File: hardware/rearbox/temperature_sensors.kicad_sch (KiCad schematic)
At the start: 15 parts

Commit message: Changed power section
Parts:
- gave numbers to parts that had none: 9
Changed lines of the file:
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@@
 (kicad_sch
-	(version 20231120)
+	(version 20250114)
 	(generator "eeschema")
-	(generator_version "8.0")
+	(generator_version "9.0")
 	(paper "A4")
 	(title_block
@@
 		(comment 1 "Reviewer:")
 	)
+	(text "G = 2\nR_{F} = 4k7\nR_{G} = 4k7"
+		(exclude_from_sim no)
+		(at 234.95 69.85 0)
+		(effects
+			(font
+				(size 1.27 1.27)
+			)
+			(justify left bottom)
+		)
+	)
+	(text "G = 2\nR_{F} = 4k7\nR_{G} = 4k7"
+		(exclude_from_sim no)
+		(at 234.95 146.05 0)
+		(effects
+			(font
+				(size 1.27 1.27)
+			)
+			(justify left bottom)
+		)
+	)
+	(text "NTC\n2k"
+		(exclude_from_sim no)
+		(at 178.435 59.055 0)
+		(effects
+			(font
+				(size 1.27 1.27)
+			)
+			(justify right bottom)
+		)
+	)
+	(text "NTC\n2k"
+		(exclude_from_sim no)
+		(at 178.435 97.155 0)
+		(effects
+			(font
+				(size 1.27 1.27)
+			)
+			(justify right bottom)
+		)
+	)
+	(text "G = 2\nR_{F} = 4k7\nR_{G} = 4k7"
+		(exclude_from_sim no)
+		(at 234.95 107.95 0)
+		(effects
+			(font
+				(size 1.27 1.27)
+			)
+			(justify left bottom)
+		)
+	)
+	(text "NTC\n2k"
+		(exclude_from_sim no)
+		(at 178.435 135.255 0)
+		(effects
+			(font
+				(size 1.27 1.27)
+			)
+			(justify right bottom)
+		)
+	)
+	(text_box "Resistance range:\n2480 to 435 Ω\n(20 to 70 °C)\n\nOptimum value of the upper resistor in the divider:\nR = sqrt(2480 * 435) ≈ 1 kΩ\n\nOutput range:\n0.237 V to 1.867 V"
+		(exclude_from_sim no)
+		(at 22.86 134.62 0)
+		(size 31.75 22.86)
+		(margins 0.9524 0.9524 0.9524 0.9524)
+		(stroke
+			(width -0.0001)
+			(type default)
+		)
+		(fill
+			(type none)
+		)
+		(effects
+			(font
+				(size 1.27 1.27)
+			)
+			(justify left top)
+		)
+	)
+	(text_box "Sensor: Bosch 0 261 230 340\nOEM ID: SH01-18-541\nRange: -40 °C to 140 °C\n\nhttps://www.efisolutions.com.au/bosch-fluid-pressure-and-temperature-sensor-pst-f1"
+		(exclude_from_sim no)
+		(at 22.86 115.57 0)
+		(size 90.17 11.43)
+		(margins 0.9524 0.9524 0.9524 0.9524)
+		(stroke
+			(width -0.0001)
+			(type default)
+		)
+		(fill
+			(type none)
+		)
+		(effects
+			(font
+				(size 1.27 1.27)
+			)
+			(justify left top)
+		)
+	)
 	(junction
 		(at 195.58 52.07)
@@
 			"AAAAAEASAOEOAAAAAABAEgDhDgAAAAAAQBIA4Q4AAAAAAEASAOEOAAAAAABAEgDhDgAAAAAAQBIA"
 			"4Q4AAAAAAEASAOEOAAAAAABAEgDhDgAAAAAAQBIA4Q4AAAAAAEASAOEOAAAAAABAEgDhDgAAAAAA"
-			"QBLw/9uJrOufjjWHAAAAAElFTkSuQmCC"
-		)
-	)
-	(text_box "Resistance range:\n2480 to 435 Ω\n(20 to 70 °C)\n\nOptimum value of the upper resistor in the divider:\nR = sqrt(2480 * 435) ≈ 1 kΩ\n\nOutput range:\n0.237 V to 1.867 V"
-		(exclude_from_sim no)
-		(at 22.86 134.62 0)
-		(size 31.75 22.86)
-		(stroke
-			(width -0.0001)
-			(type default)
-		)
-		(fill
-			(type none)
-		)
-		(effects
-			(font
-				(size 1.27 1.27)
-			)
-			(justify left top)
-		)
-	)
-	(text_box "Sensor: Bosch 0 261 230 340\nOEM ID: SH01-18-541\nRange: -40 °C to 140 °C\n\nhttps://www.efisolutions.com.au/bosch-fluid-pressure-and-temperature-sensor-pst-f1"
-		(exclude_from_sim no)
-		(at 22.86 115.57 0)
-		(size 90.17 11.43)
-		(stroke
-			(width -0.0001)
-			(type default)
-		)
-		(fill
-			(type none)
-		)
-		(effects
-			(font
-				(size 1.27 1.27)
-			)
-			(justify left top)
-		)
-	)
-	(text "G = 2\nR_{F} = 4k7\nR_{G} = 4k7"
-		(exclude_from_sim no)
-		(at 234.95 69.85 0)
-		(effects
-			(font
-				(size 1.27 1.27)
-			)
-			(justify left bottom)
-		)
-	)
-	(text "G = 2\nR_{F} = 4k7\nR_{G} = 4k7"
-		(exclude_from_sim no)
-		(at 234.95 146.05 0)
-		(effects
-			(font
-				(size 1.27 1.27)
-			)
-			(justify left bottom)
-		)
-	)
-	(text "NTC\n2k"
-		(exclude_from_sim no)
-		(at 178.435 59.055 0)
-		(effects
-			(font
-				(size 1.27 1.27)
-			)
-			(justify right bottom)
-		)
-	)
-	(text "NTC\n2k"
-		(exclude_from_sim no)
-		(at 178.435 97.155 0)
-		(effects
-			(font
-				(size 1.27 1.27)
-			)
-			(justify right bottom)
-		)
-	)
-	(text "G = 2\nR_{F} = 4k7\nR_{G} = 4k7"
-		(exclude_from_sim no)
-		(at 234.95 107.95 0)
-		(effects
-			(font
-				(size 1.27 1.27)
-			)
-			(justify left bottom)
-		)
-	)
-	(text "NTC\n2k"
-		(exclude_from_sim no)
-		(at 178.435 135.255 0)
-		(effects
-			(font
-				(size 1.27 1.27)
-			)
-			(justify right bottom)
+			"QBLw/9uJrOufjjWHAAAAAElFTkSuQmCCMQBwAFgAbABnAHcAdwA2AFEAbQBaAG4ATQBUAGwAZwBu"
+			"AEwARAB3ADgATQBwAFIAMgBzAG0AWQBGAEUAQQBpAHAATgBPAFAASQByAFMATgBJAHkAcQBqAFIA"
+			"YQBGAGUAVABaAEQAawBKAEQASwBEAEUAQQB6AGcAYQBWAGYAVgB5AEsAUwBKAHoAcAA5ACsANgAy"
+			"AHEANQBrAEMAUAB0AGgAeQBWAGcATwBUAEkAcwAvAGkAbgBUADMAdwB1AEoAVgBUAFoAcwBhAHgA"
+			"bQBMAE0AVABiADMAbgBiAEoAVwBlAGMAYwBTAGQAbABCAGoATQBXAFEASwBLADYAagBJAEUAbABM"
+			"AEMAVABRAG8AYQBHAG8ATgAyAEsAaABoAGEATgA2ADgANABrAFAAWAB2AEgAWABwAEUAawBiAEMA"
+			"cgBEAFIATABaAHAAWQBVAEUAUAB6AHcAQgArAHYAdgB1AEgAMgAxAFcAdAAwADcAUAA0ADUANwBM"
+			"AG4AbgA3AFoAbgB2ADMATAAwADEAVQBPADMANQBSAHQAZABCAFYAUQBHAEcAbQBKAFYAagA3AEYA"
+			"OQBLAHoAaQBsAEkAQgB0AFIAeABiAFoAbAA4AHIATgArACsAcQBqAHEAQwBFAGQAbABLADEAMgB0"
+			"ADQAVAB4AGMAWQAzAEgAUABoAGQAcwB0AC8AWgBDADMAcwBTAHIAWABlADEAbgBKAGkANwBtAGgA"
+			"UQBKAEgAdQArACsAcwA2AFAAcQBMAGEAUQBRAGgAYQBaAEEANgAvAHYAYgB2AC8AMwBzADgARABC"
+			"AEsAaABTAFAARgBRAGcATQAxAEIAaQB4AGIASwBuAC8ALwBzAFgAZQBjAGQAOQA3AHgATQBXAHcA"
+			"VAAyAFMANwBZAEwAaAB5AEcARABSAE8AagBRAFUAYgBOAGQAZwBSAHUAQgA3AGMAVgBjAGYAcwBM"
+			"AEwAagByAHAAQQB4ADkAOAAzAGYAUgBwAEkARQBHAHgAVgB0AGsAUwBnAFIARgBsAGkAUQBkAFgA"
+			"bABWAC8AKwA4AHIAZgBCAEsAYQBxAGkAbwBQAE0AcABxAHcAYgBwADcAYgBQAFYAYgB0ACsAOQBN"
+			"AHYARgBrAFYAcABlAEMAVABmAHMARwBTAEcALwA2AGMAcwBKAGQAYQBvAGMAdQBPADEAbABxAEsA"
+			"dwBwAEgARAArAHEAVABzAFIALwBtADkAKwAxADUAcwArAE4AeAB6AGsAUgBLADIAZABmADAAZABB"
+			"AFMASQBwAFUAdAByAGYALwBmAFIAZAB4ADUANQA1AEoASQBnAFcAOABGAHQASQBqAHMAQwBSAHMA"
+			"MQBHAFkAQwBQAEMARQBjAG8AUQBiAA=="
 		)
 	)
 	(label "N3"
 		(at 218.44 132.08 180)
-		(fields_autoplaced yes)
 		(effects
 			(font
@@
 	(label "N3"
 		(at 185.42 128.27 180)
-		(fields_autoplaced yes)
 		(effects
 			(font
@@
 	(label "N2"
 		(at 185.42 90.17 180)
-		(fields_autoplaced yes)
 		(effects
 			(font
@@
 	(label "P2"
 		(at 190.5 90.17 0)
-		(fields_autoplaced yes)
 		(effects
 			(font
@@
 	(label "N2"
 		(at 218.44 93.98 180)
-		(fields_autoplaced yes)
 		(effects
 			(font
@@
 	(label "N1"
 		(at 218.44 55.88 180)
-		(fields_autoplaced yes)
 		(effects
 			(font
@@
 	(label "N1"
 		(at 185.42 52.07 180)
-		(fields_autoplaced yes)
 		(effects
 			(font
@@
 	(label "P1"
 		(at 218.44 49.53 180)
-		(fields_autoplaced yes)
 		(effects
 			(font
@@
 	(label "P3"
 		(at 190.5 128.27 0)
-		(fields_autoplaced yes)
 		(effects
 			(font
@@
 	(label "P2"
 		(at 218.44 87.63 180)
-		(fields_autoplaced yes)
 		(effects
 			(font
@@
 	(label "P3"
 		(at 218.44 125.73 180)
-		(fields_autoplaced yes)
 		(effects
 			(font
@@
 	(label "P1"
 		(at 190.5 52.07 0)
-		(fields_autoplaced yes)
 		(effects
 			(font
@@
 		(shape output)
 		(at 252.73 125.73 0)
-		(fields_autoplaced yes)
 		(effects
 			(font
@@
 		(shape input)
 		(at 173.99 128.27 180)
-		(fields_autoplaced yes)
 		(effects
 			(font
@@
 		(shape output)
 		(at 252.73 49.53 0)
-		(fields_autoplaced yes)
 		(effects
 			(font
@@
 		(shape input)
 		(at 173.99 90.17 180)
-		(fields_autoplaced yes)
 		(effects
 			(font
@@
 		(shape output)
 		(at 252.73 87.63 0)
-		(fields_autoplaced yes)
 		(effects
 			(font
@@
 		(shape input)
 		(at 173.99 52.07 180)
-		(fields_autoplaced yes)
 		(effects
 			(font
@@
 		(on_board yes)
 		(dnp no)
-		(property "Reference" "R?"
+		(property "Reference" "R100"
 			(at 197.358 120.7516 0)
 			(effects
@@
 		(on_board yes)
 		(dnp no)
-		(property "Reference" "R?"
+		(property "Reference" "R95"
 			(at 178.562 120.7516 0)
 			(effects
@@
 		(on_board yes)
 		(dnp no)
-		(property "Reference" "R?"
+		(property "Reference" "R94"
 			(at 178.562 82.6516 0)
 			(effects
@@
 		(on_board yes)
 		(dnp no)
-		(property "Reference" "R?"
+		(property "Reference" "R98"
 			(at 197.358 82.6516 0)
 			(effects
@@
 		(on_board yes)
 		(dnp no)
-		(property "Reference" "#PWR?"
+		(property "Reference" "#PWR0192"
 			(at 187.96 68.58 0)
 			(effects
@@
 		(on_board yes)
 		(dnp no)
-		(property "Reference" "#PWR?"
+		(property "Reference" "#PWR0196"
 			(at 187.96 144.78 0)
 			(effects
@@
 		(on_board yes)
 		(dnp no)
-		(property "Reference" "R?"
+		(property "Reference" "R97"
 			(at 197.358 54.7116 0)
 			(effects
@@
 		(on_board yes)
 		(dnp no)
-		(property "Reference" "#PWR?"
+		(property "Reference" "#PWR0194"
 			(at 187.96 106.68 0)
 			(effects
@@
 		(on_board yes)
 		(dnp no)
-		(property "Reference" "R?"
+		(property "Reference" "R96"
 			(at 197.358 44.5516 0)
 			(effects
@@
 		(on_board yes)
 		(dnp no)
-		(property "Reference" "R?"
+		(property "Reference" "R101"
 			(at 197.358 130.9116 0)
 			(effects
@@
 		(on_board yes)
 		(dnp no)
-		(property "Reference" "R?"
+		(property "Reference" "R99"
 			(at 197.358 92.8116 0)
 			(effects
@@
 		(on_board yes)
 		(dnp no)
-		(property "Reference" "R?"
+		(property "Reference" "R93"
 			(at 178.562 44.5516 0)
 			(effects
@@
 		(at 227.33 121.92)
 		(size 24.13 13.97)
+		(exclude_from_sim no)
+		(in_bom yes)
+		(on_board yes)
+		(dnp no)
 		(stroke
 			(width 0.1524)
@@
 		(at 227.33 45.72)
 		(size 24.13 13.97)
+		(exclude_from_sim no)
+		(in_bom yes)
+		(on_board yes)
+		(dnp no)
 		(stroke
 			(width 0.1524)
@@
 		(at 227.33 83.82)
 		(size 24.13 13.97)
+		(exclude_from_sim no)
+		(in_bom yes)
+		(on_board yes)
+		(dnp no)
 		(stroke
 			(width 0.1524)

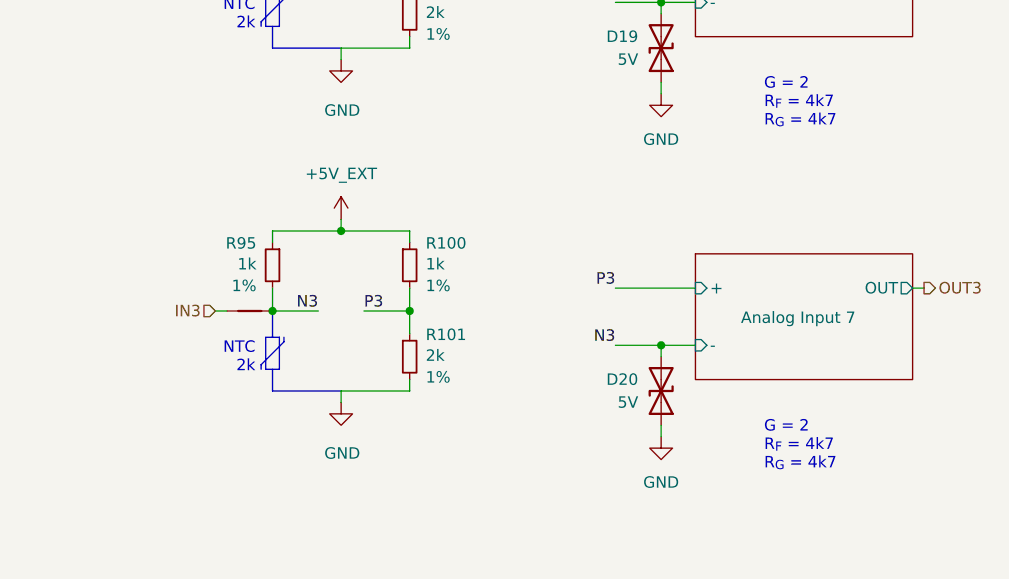
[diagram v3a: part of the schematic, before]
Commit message: Deleted measurement systems for new iteration
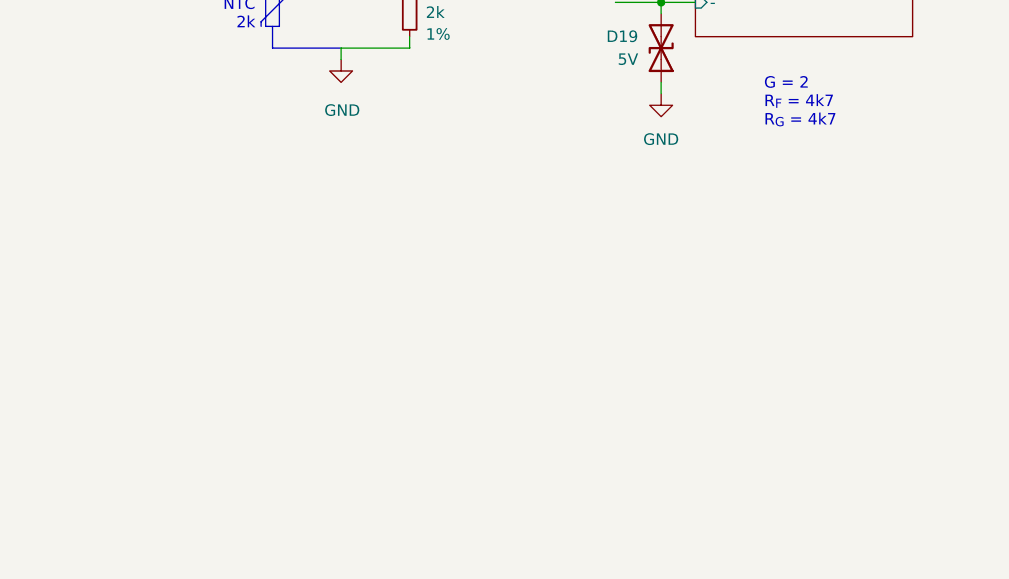
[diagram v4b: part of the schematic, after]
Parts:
- removed D20: 5V, Diode_SMD:D_SOD-523, symbol Device:D_TVS
- removed NT3: NetTie_2, Local_Library:NetTie-2_SMD_Pad0.2mm, symbol Device:NetTie_2
- removed R100, R95: 1k, Resistor_SMD:R_0603_1608Metric, symbol Device:R_Small
- removed R101: 2k, Resistor_SMD:R_0603_1608Metric, symbol Device:R_Small
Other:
- removed sheet Analog Input 7
